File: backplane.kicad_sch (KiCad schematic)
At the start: 0 parts

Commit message: [#56643] Create buses for interfaces, assign buses to blocks
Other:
- company: (none) -> Antmicro Ltd.
- title: (none) -> Com Express 7 baseboard
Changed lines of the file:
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@@
 (kicad_sch (version 20230121) (generator eeschema)
-  (paper "A4")
+  (paper "A3")
+  (title_block
+    (title "Com Express 7 baseboard")
+    (date "2024-03-22")
+    (rev "1.0.0")
+    (company "Antmicro Ltd.")
+  )
   (hierarchical_label "USB{USB}" (shape input) (at 48.26 88.9 180) (fields_autoplaced)
     (effects (font (size 1.27 1.27)) (justify right))

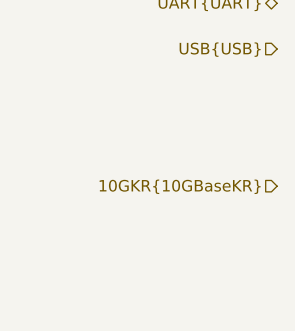
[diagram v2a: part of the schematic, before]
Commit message: [#57056] Update PCIe lane assignment, drop 2nd OCuLink
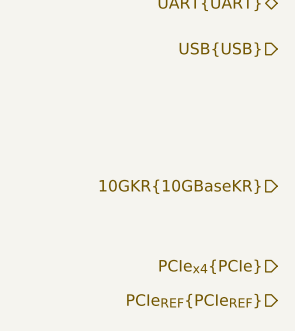
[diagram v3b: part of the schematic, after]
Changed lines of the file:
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@@
+    (effects (font (size 1.27 1.27)) (justify right))
+  )
+  (hierarchical_label "PCIe_{REF}{PCIe_{REF}}" (shape input) (at 48.26 116.84 180) (fields_autoplaced)
     (effects (font (size 1.27 1.27)) (justify right))
   )
@@
     (effects (font (size 1.27 1.27)) (justify right))
   )
+  (hierarchical_label "PCIe_{x4}{PCIe}" (shape input) (at 48.26 113.03 180) (fields_autoplaced)
+    (effects (font (size 1.27 1.27)) (justify right))
+  )

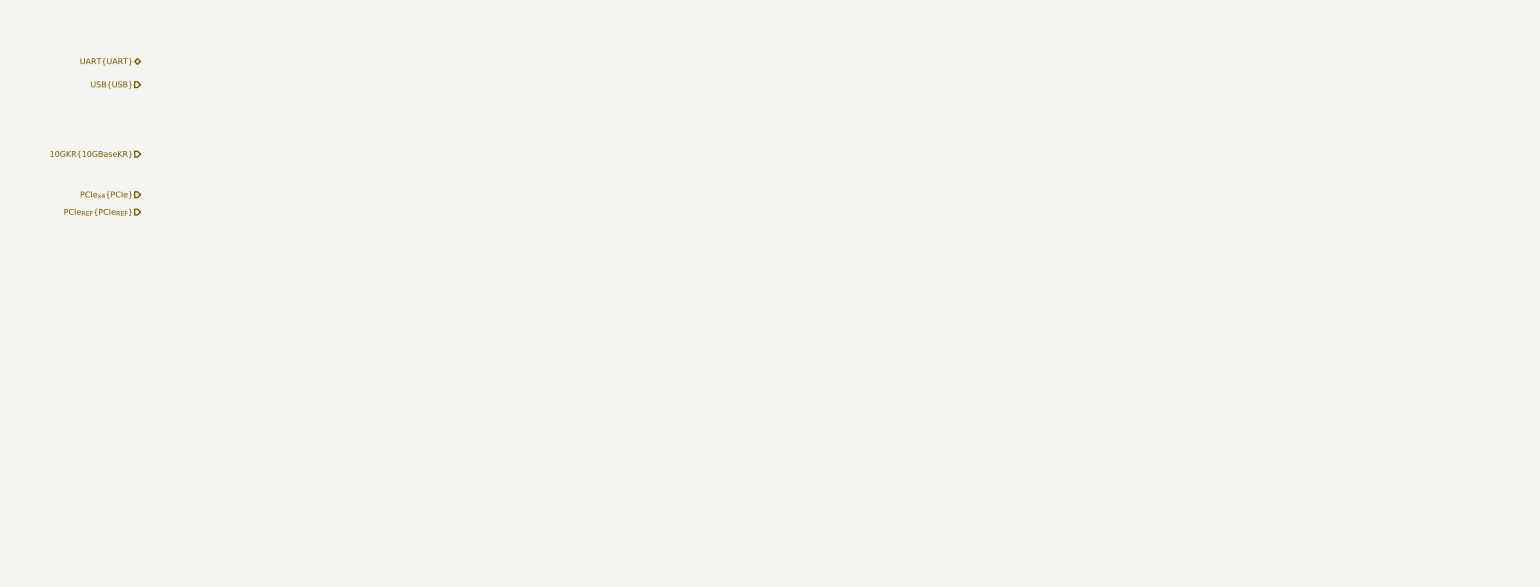
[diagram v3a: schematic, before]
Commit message: [#57056] Add backplane connector
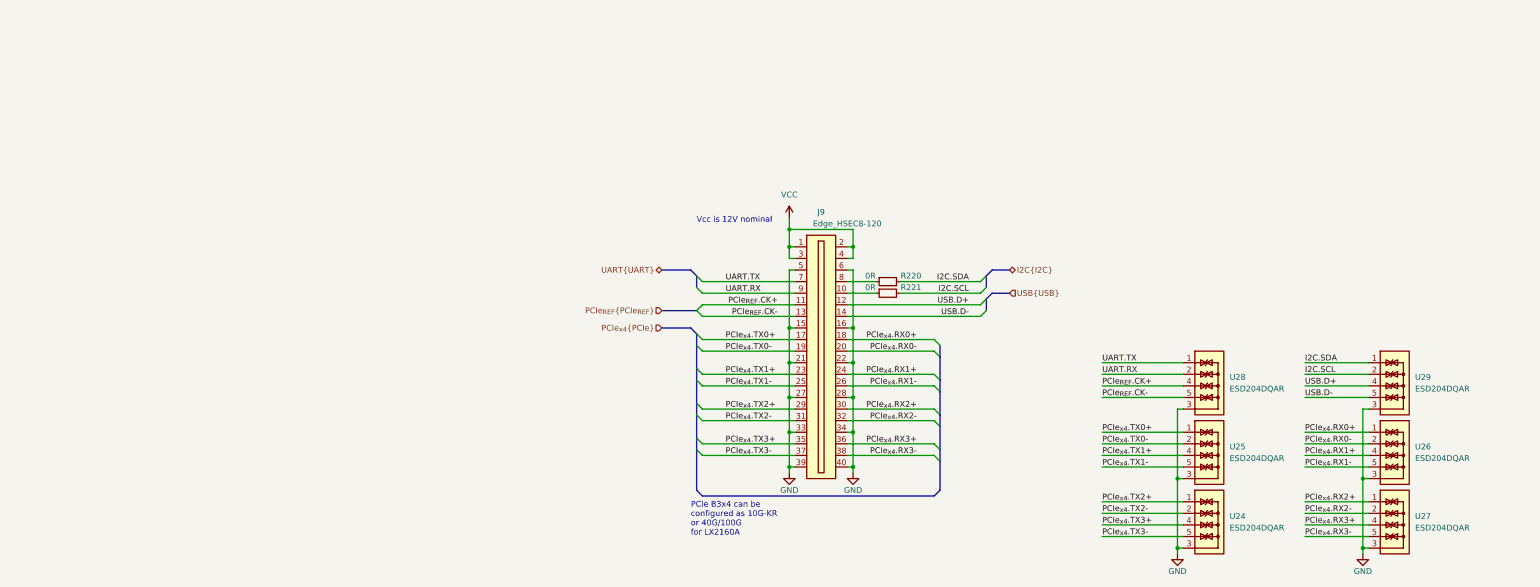
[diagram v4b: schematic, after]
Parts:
- added J9: Edge_HSEC8-120, symbol antmicroEdgeConnectors:Edge_HSEC8-120
- added R220, R221: R_0R_0402, antmicro-footprints:R_0402_1005Metric, symbol antmicroResistors0402:R_0R_0402
- added U24, U25, U26, U27, U28, U29: ESD204DQAR, antmicro-footprints:USON-10_2.5x1mm_P0.5mm, symbol antmicroTVSDiodes:ESD204DQAR
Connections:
- new net: J9.8, R220.1
- new net: J9.10, R221.1
- new net GND: J9.15, J9.16, J9.21, J9.22, J9.27, J9.28, J9.33, J9.34, J9.39, J9.40, J9.5, J9.6, U24.3, U24.8, U25.3, U25.8, U26.3, U26.8, U27.3, U27.8, U28.3, U28.8, U29.3, U29.8
- new net I2C.SCL: R221.2, U29.2, U29.9
- new net I2C.SDA: R220.2, U29.1, U29.10
- new net PCIe_{REF}.CK+: J9.11, U28.4, U28.7
- new net PCIe_{REF}.CK-: J9.13, U28.5, U28.6
- new net PCIe_{x4}.RX0+: J9.18, U26.1, U26.10
- new net PCIe_{x4}.RX0-: J9.20, U26.2, U26.9
- new net PCIe_{x4}.RX1+: J9.24, U26.4, U26.7
- new net PCIe_{x4}.RX1-: J9.26, U26.5, U26.6
- new net PCIe_{x4}.RX2+: J9.30, U27.1, U27.10
- new net PCIe_{x4}.RX2-: J9.32, U27.2, U27.9
- new net PCIe_{x4}.RX3+: J9.36, U27.4, U27.7
- new net PCIe_{x4}.RX3-: J9.38, U27.5, U27.6
- new net PCIe_{x4}.TX0+: J9.17, U25.1, U25.10
- new net PCIe_{x4}.TX0-: J9.19, U25.2, U25.9
- new net PCIe_{x4}.TX1+: J9.23, U25.4, U25.7
- new net PCIe_{x4}.TX1-: J9.25, U25.5, U25.6
- new net PCIe_{x4}.TX2+: J9.29, U24.1, U24.10
- new net PCIe_{x4}.TX2-: J9.31, U24.2, U24.9
- new net PCIe_{x4}.TX3+: J9.35, U24.4, U24.7
- new net PCIe_{x4}.TX3-: J9.37, U24.5, U24.6
- new net UART.RX: J9.9, U28.2, U28.9
- new net UART.TX: J9.7, U28.1, U28.10
- new net USB.D+: J9.12, U29.4, U29.7
- new net USB.D-: J9.14, U29.5, U29.6
- new net VCC: J9.1, J9.2, J9.3, J9.4
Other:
- note added: "PCIe B3x4 can be configured as 10G-KR or 40G/100G for LX2160A"
- note added: "Vcc is 12V nominal"

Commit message: [#58137] Update backplane connector pinout
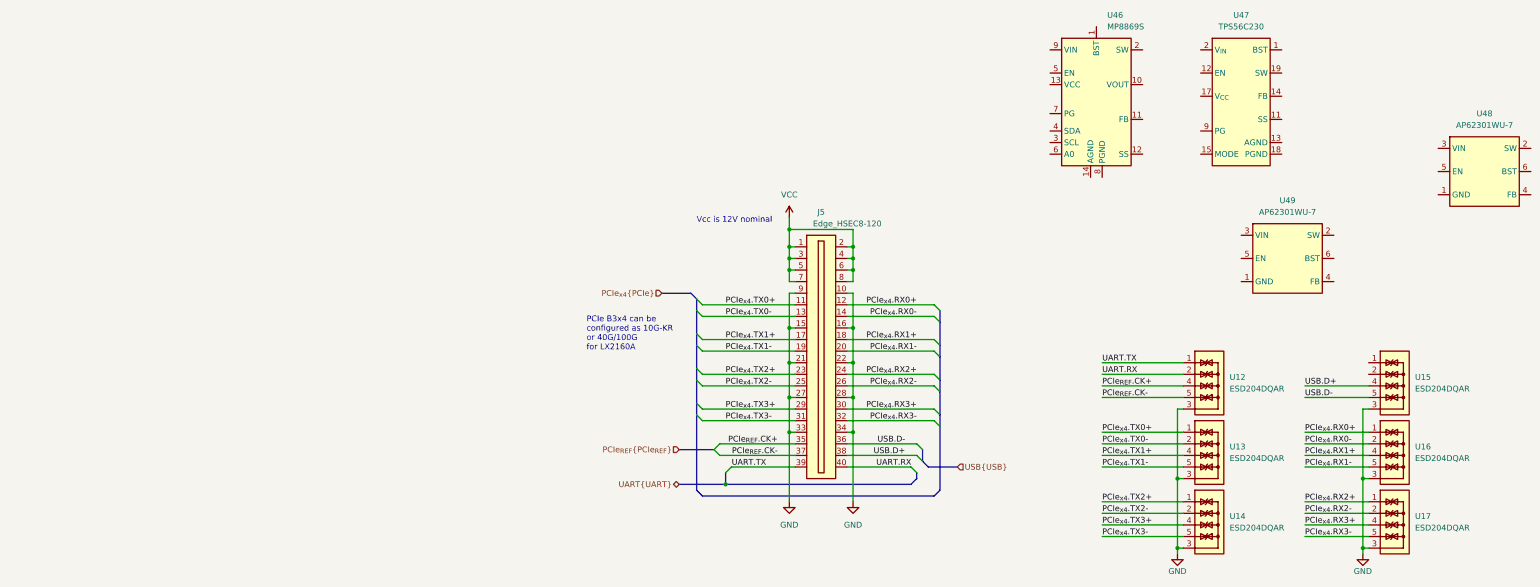
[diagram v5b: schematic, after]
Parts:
- removed R220, R221: R_0R_0402, antmicro-footprints:R_0402_1005Metric, symbol antmicroResistors0402:R_0R_0402
- added U46: MP8869S, antmicro-footprints:MPS_QFN-14_MP8869S, symbol antmicroPMICVoltageRegulatorsDCDCSwitchingRegulators:MP8869S
- added U47: TPS56C230, antmicro-footprints:QFN-20-1EP_3x3mm_P0.45mm, symbol antmicroDCDCConverters:TPS56C230
- added U48, U49: AP62301_TSOT, antmicro-footprints:TSOT23-6, symbol antmicroDCDCConverters:AP62301_TSOT
- renumbered J9 to J5, U28 to U12, U25 to U13, U24 to U14, U29 to U15, U26 to U16, U27 to U17
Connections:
- net GND: now also J5.10, J5.9; no longer J5.39, J5.40, J5.5, J5.6
- net PCIe_{REF}.CK+: now also J5.35; no longer J5.11
- net PCIe_{REF}.CK-: now also J5.37; no longer J5.13
- net PCIe_{x4}.RX0+: now also J5.12; no longer J5.18
- net PCIe_{x4}.RX0-: now also J5.14; no longer J5.20
- net PCIe_{x4}.RX1+: now also J5.18; no longer J5.24
- net PCIe_{x4}.RX1-: now also J5.20; no longer J5.26
- net PCIe_{x4}.RX2+: now also J5.24; no longer J5.30
- net PCIe_{x4}.RX2-: now also J5.26; no longer J5.32
- net PCIe_{x4}.RX3+: now also J5.30; no longer J5.36
- net PCIe_{x4}.RX3-: now also J5.32; no longer J5.38
- net PCIe_{x4}.TX0+: now also J5.11; no longer J5.17
- net PCIe_{x4}.TX0-: now also J5.13; no longer J5.19
- net PCIe_{x4}.TX1+: now also J5.17; no longer J5.23
- net PCIe_{x4}.TX1-: now also J5.19; no longer J5.25
- net PCIe_{x4}.TX2+: now also J5.23; no longer J5.29
- net PCIe_{x4}.TX2-: now also J5.25; no longer J5.31
- net PCIe_{x4}.TX3+: now also J5.29; no longer J5.35
- net PCIe_{x4}.TX3-: now also J5.31; no longer J5.37
- net UART.RX: now also J5.40; no longer J5.9
- net UART.TX: now also J5.39; no longer J5.7
- net USB.D+: now also J5.38; no longer J5.12
- net USB.D-: now also J5.36; no longer J5.14
- net VCC: now also J5.5, J5.6, J5.7, J5.8
- net I2C.SCL: no longer names the net of U15.2, U15.9
- net I2C.SDA: no longer names the net of U15.1, U15.10
- new net: U47.18 (PGND), U47.21 (PGND), U47.7 (PGND), U47.8 (PGND)
- new net: U47.19 (SW), U47.20 (SW), U47.6 (SW)
- new net: U47.2 (V_{IN}), U47.3 (V_{IN}), U47.4 (V_{IN}), U47.5 (V_{IN})

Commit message: Update symbols from the library
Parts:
- removed J5: Edge_HSEC8-120, symbol antmicroEdgeConnectors:Edge_HSEC8-120
- added J5: Edge_Conn_HSEC8-120, antmicro-footprints:Edge_Conn_HSEC8_120, symbol antmicroEdgeConnectors:Edge_Conn_HSEC8-120
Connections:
- net GND: now also J5.10, J5.15, J5.16, J5.21, J5.22, J5.27, J5.28, J5.33, J5.34, J5.9
- net PCIe_{REF}.CK+: now also J5.35
- net PCIe_{REF}.CK-: now also J5.37
- net PCIe_{x4}.RX0+: now also J5.12
- net PCIe_{x4}.RX0-: now also J5.14
- net PCIe_{x4}.RX1+: now also J5.18
- net PCIe_{x4}.RX1-: now also J5.20
- net PCIe_{x4}.RX2+: now also J5.24
- net PCIe_{x4}.RX2-: now also J5.26
- net PCIe_{x4}.RX3+: now also J5.30
- net PCIe_{x4}.RX3-: now also J5.32
- net PCIe_{x4}.TX0+: now also J5.11
- net PCIe_{x4}.TX0-: now also J5.13
- net PCIe_{x4}.TX1+: now also J5.17
- net PCIe_{x4}.TX1-: now also J5.19
- net PCIe_{x4}.TX2+: now also J5.23
- net PCIe_{x4}.TX2-: now also J5.25
- net PCIe_{x4}.TX3+: now also J5.29
- net PCIe_{x4}.TX3-: now also J5.31
- net UART.RX: now also J5.40
- net UART.TX: now also J5.39
- net USB.D+: now also J5.38
- net USB.D-: now also J5.36
- net VCC: now also J5.1, J5.2, J5.3, J5.4, J5.5, J5.6, J5.7, J5.8
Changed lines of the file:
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@@
+    )
+  )
+  (symbol (lib_id "antmicroEdgeConnectors:Edge_Conn_HSEC8-120") (at 191.77 124.46 0) (unit 1)
+    (in_bom yes) (on_board yes) (dnp no)
+    (property "Reference" "J5" (at 197.485 116.84 0)
+      (effects (font (size 1.27 1.27) (thickness 0.15)))
+    )
+    (property "Value" "Edge_Conn_HSEC8-120" (at 200.66 119.38 0)
+      (effects (font (size 1.27 1.27) (thickness 0.15)))
+    )
+    (property "Footprint" "antmicro-footprints:Edge_Conn_HSEC8_120" (at 217.17 132.08 0)
+      (effects (font (size 1.27 1.27) (thickness 0.15)) (justify left bottom) hide)
+    )
+    (property "Datasheet" "https://suddendocs.samtec.com/prints/hsec8-1xxx-xx-xx-dv-x-xx-footprint.pdf" (at 217.17 134.62 0)
+      (effects (font (size 1.27 1.27) (thickness 0.15)) (justify left bottom) hide)
+    )
+    (property "Author" "Antmicro" (at 217.17 137.16 0)
+      (effects (font (size 1.27 1.27) (thickness 0.15)) (justify left bottom) hide)
+    )
+    (property "License" "Apache-2.0" (at 217.17 139.7 0)
+      (effects (font (size 1.27 1.27) (thickness 0.15)) (justify left bottom) hide)
+    )
+    (pin "22")
+    (pin "16")
+    (pin "9")
+    (pin "20")
+    (pin "39")
+    (pin "15")
+    (pin "14")
+    (pin "11")
+    (pin "33")
+    (pin "19")
+    (pin "28")
+    (pin "21")
+    (pin "2")
+    (pin "3")
+    (pin "25")
+    (pin "7")
+    (pin "29")
+    (pin "18")
+    (pin "4")
+    (pin "24")
+    (pin "6")
+    (pin "34")
+    (pin "37")
+    (pin "36")
+    (pin "12")
+    (pin "23")
+    (pin "5")
+    (pin "40")
+    (pin "27")
+    (pin "26")
+    (pin "32")
+    (pin "31")
+    (pin "35")
+    (pin "1")
+    (pin "38")
+    (pin "10")
+    (pin "30")
+    (pin "8")
+    (pin "17")
+    (pin "13")
+    (instances
+      (project "com-express-7-baseboard"
+        (path "/1b8c34da-dad5-4b0b-8c4b-45db766c4dfa/55405a83-d274-4fdb-aba5-7f854fcb14c7"
+          (reference "J5") (unit 1)
+        )
+      )
     )
   )
@@
         )
       )
-    )
-  )
-  (symbol (lib_id "antmicroEdgeConnectors:Edge_HSEC8-120") (at 191.77 124.46 0) (unit 1)
-    (in_bom yes) (on_board yes) (dnp no)
-    (property "Reference" "J5" (at 197.485 116.84 0)
-      (effects (font (size 1.27 1.27)))
-    )
-    (property "Value" "Edge_HSEC8-120" (at 203.2 119.38 0)
-      (effects (font (size 1.27 1.27)))
-    )
-    (property "Footprint" "" (at 237.49 99.06 0)
-      (effects (font (size 1.27 1.27)) hide)
-    )
-    (property "Datasheet" "https://suddendocs.samtec.com/prints/hsec8-1xxx-xx-xx-dv-x-xx-footprint.pdf" (at 237.49 99.06 0)
-      (effects (font (size 1.27 1.27)) hide)
-    )
-    (pin "16")
-    (pin "27")
-    (pin "36")
-    (pin "22")
-    (pin "37")
-    (pin "40")
-    (pin "6")
-    (pin "25")
-    (pin "24")
-    (pin "33")
-    (pin "4")
-    (pin "5")
-    (pin "38")
-    (pin "2")
-    (pin "10")
-    (pin "9")
-    (pin "11")
-    (pin "20")
-    (pin "14")
-    (pin "15")
-    (pin "23")
-    (pin "17")
-    (pin "31")
-    (pin "1")
-    (pin "3")
-    (pin "39")
-    (pin "8")
-    (pin "12")
-    (pin "35")
-    (pin "29")
-    (pin "19")
-    (pin "18")
-    (pin "28")
-    (pin "32")
-    (pin "34")
-    (pin "7")
-    (pin "30")
-    (pin "26")
-    (pin "13")
-    (pin "21")
-    (instances
-      (project "com-express-7-baseboard"
-        (path "/1b8c34da-dad5-4b0b-8c4b-45db766c4dfa/55405a83-d274-4fdb-aba5-7f854fcb14c7"
-          (reference "J5") (unit 1)
-        )
-      )
